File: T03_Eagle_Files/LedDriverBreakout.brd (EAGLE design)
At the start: 100 x 80 mm, 3 parts, among them U1 TPS61161ADRVT, X1 22-23-2031, X2 22-23-2031

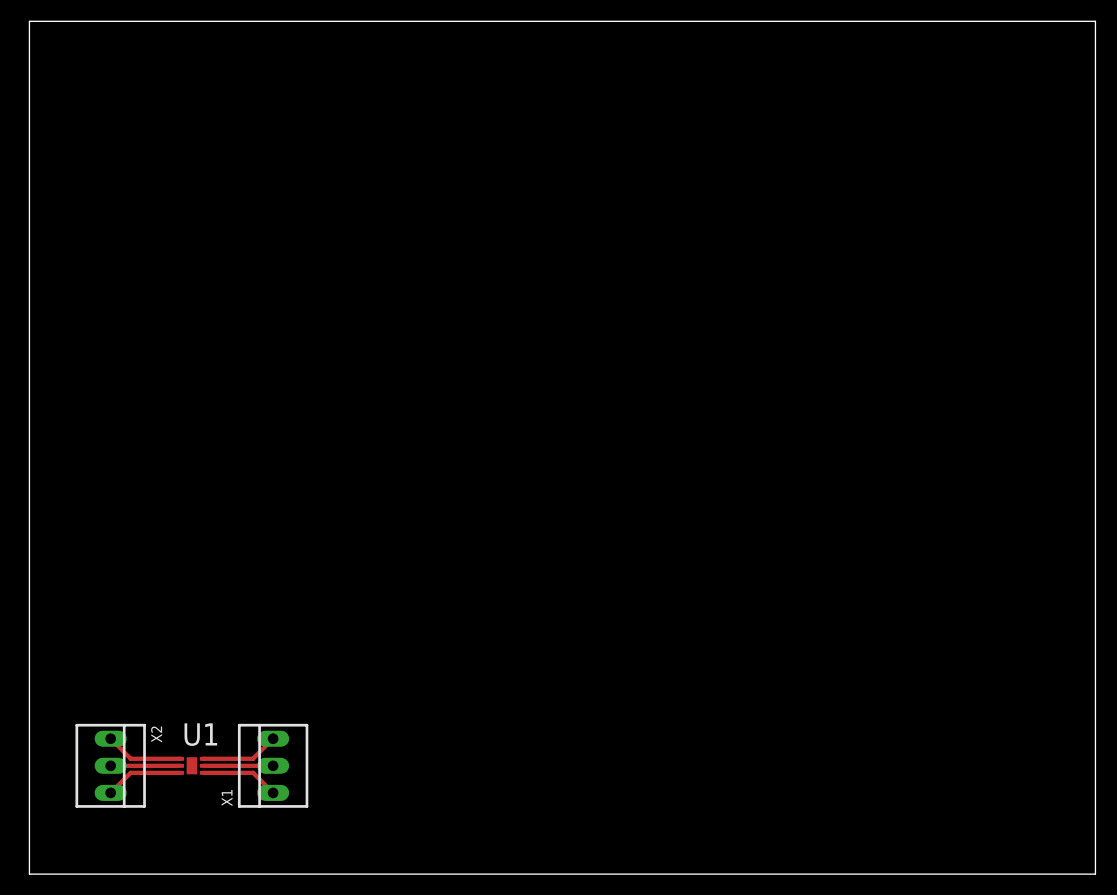
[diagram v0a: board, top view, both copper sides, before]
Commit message: Cleaned up LED driver breakoout for machining
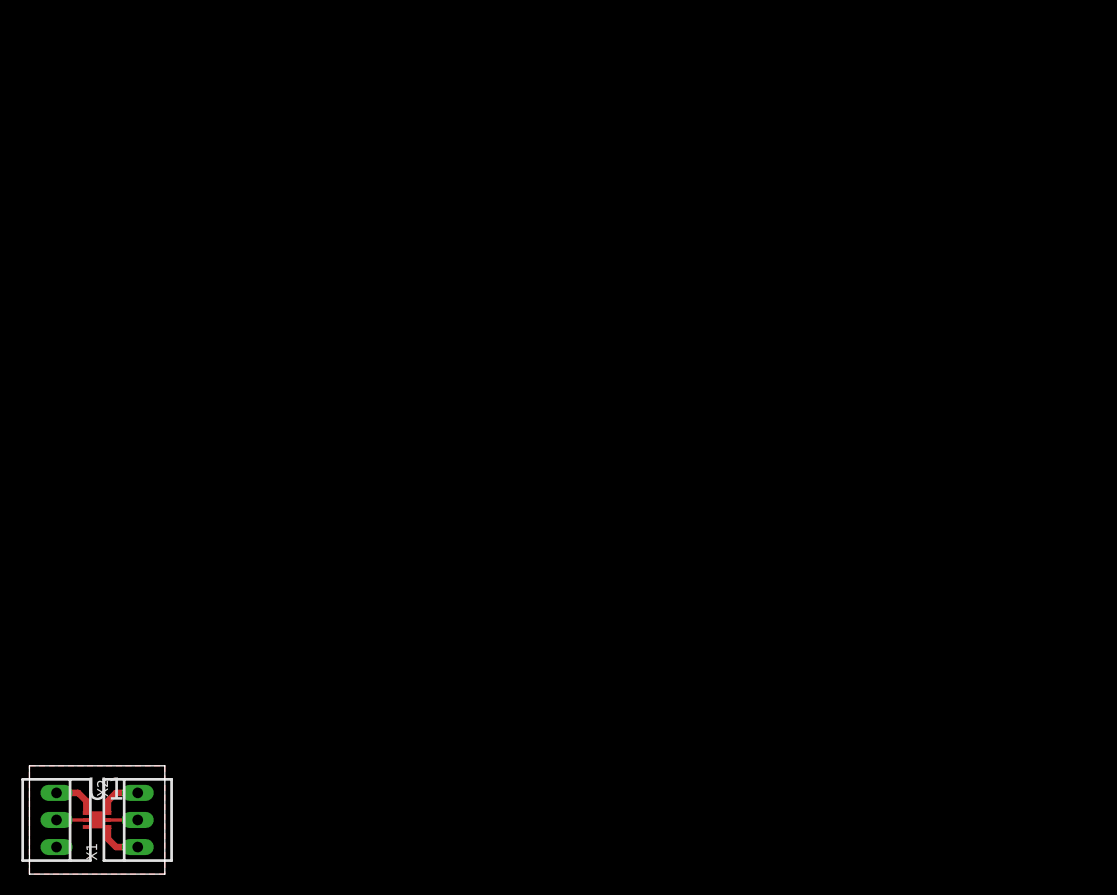
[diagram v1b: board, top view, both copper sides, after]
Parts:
- moved X1 13.7 mm to (10.2, 5.08)
- moved U1 10.2 mm to (6.35, 5.08)
- moved X2 7.18 mm to (2.54, 5.08)
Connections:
- net GND: now also U1.7
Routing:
- net GND: track 7.36 -> 0.00 mm
- net COMP: track 6.58 -> 2.77 mm
- net CTRL: track 6.58 -> 2.77 mm
- net FB: track 7.36 -> 4.24 mm
- net VIN: track 7.36 -> 4.24 mm
- net SW: track 7.36 -> 4.24 mm
- added copper zone on layer 1, net GND
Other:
- board size 100 x 80 mm -> 12.7 x 10.2 mm
